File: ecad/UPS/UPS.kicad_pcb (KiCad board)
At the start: 4 copper layers, 177.8 x 139.7 mm, 159 parts, among them J1 Barrel_Jack, J2 Conn_01x02_Socket, J3 USB_C_Receptacle_USB2.0_16P, J4 PROG, Q2 Q_PMOS_DGS, Q3 IRLR7843TRPBF, Q6 Q_NMOS_GDS, Q7 Q_NMOS_GDS, Q8 Q_NMOS_GDS, Q9 Q_NMOS_GDS, SW1 SW_Push, SW2 SW_Push, SW3 SW_DPDT_x2, U1 BQ25730RSNR, U2 MPQ5031GRE-0001-AEC1-P, U3 L78L05_SOT89, U4 STM32L152RCT6, U5 AP2112K-3.3TRG1

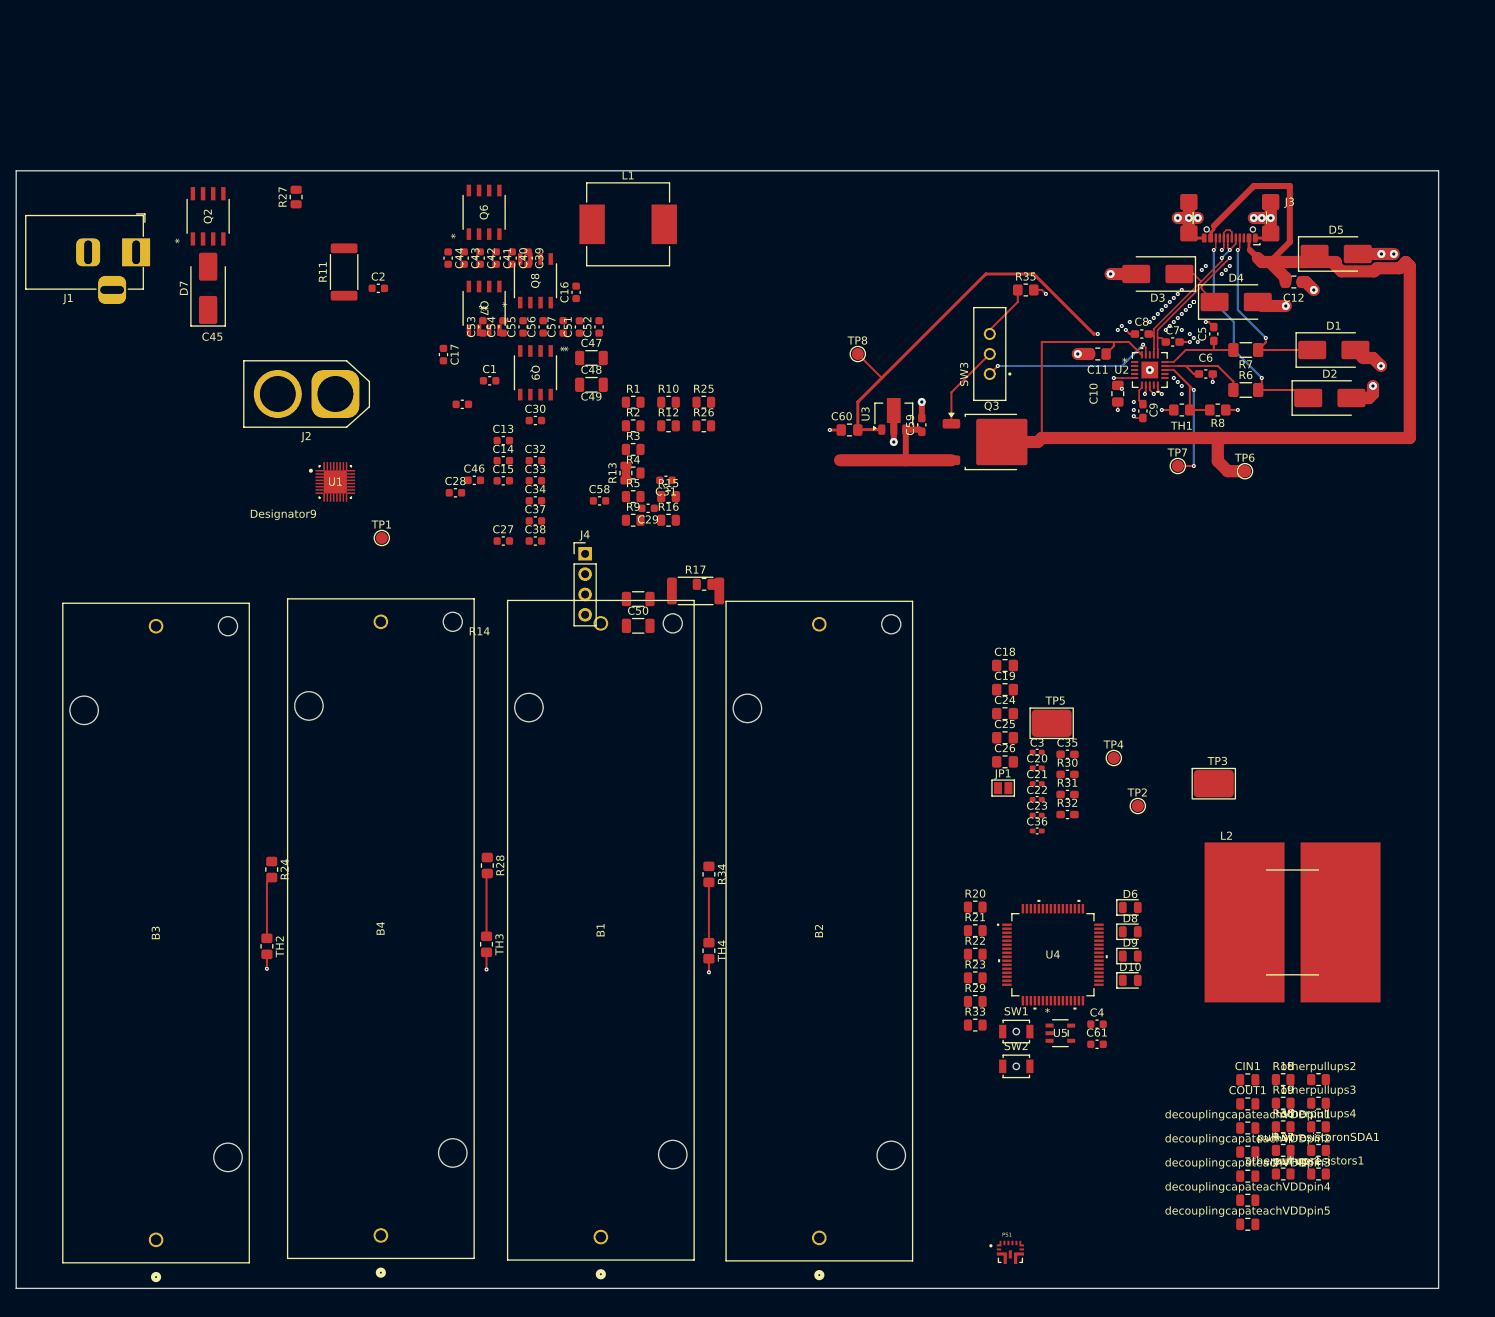
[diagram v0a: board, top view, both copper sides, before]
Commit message: Did some routing, need to figure out how to route to BQ while appeasing DRC
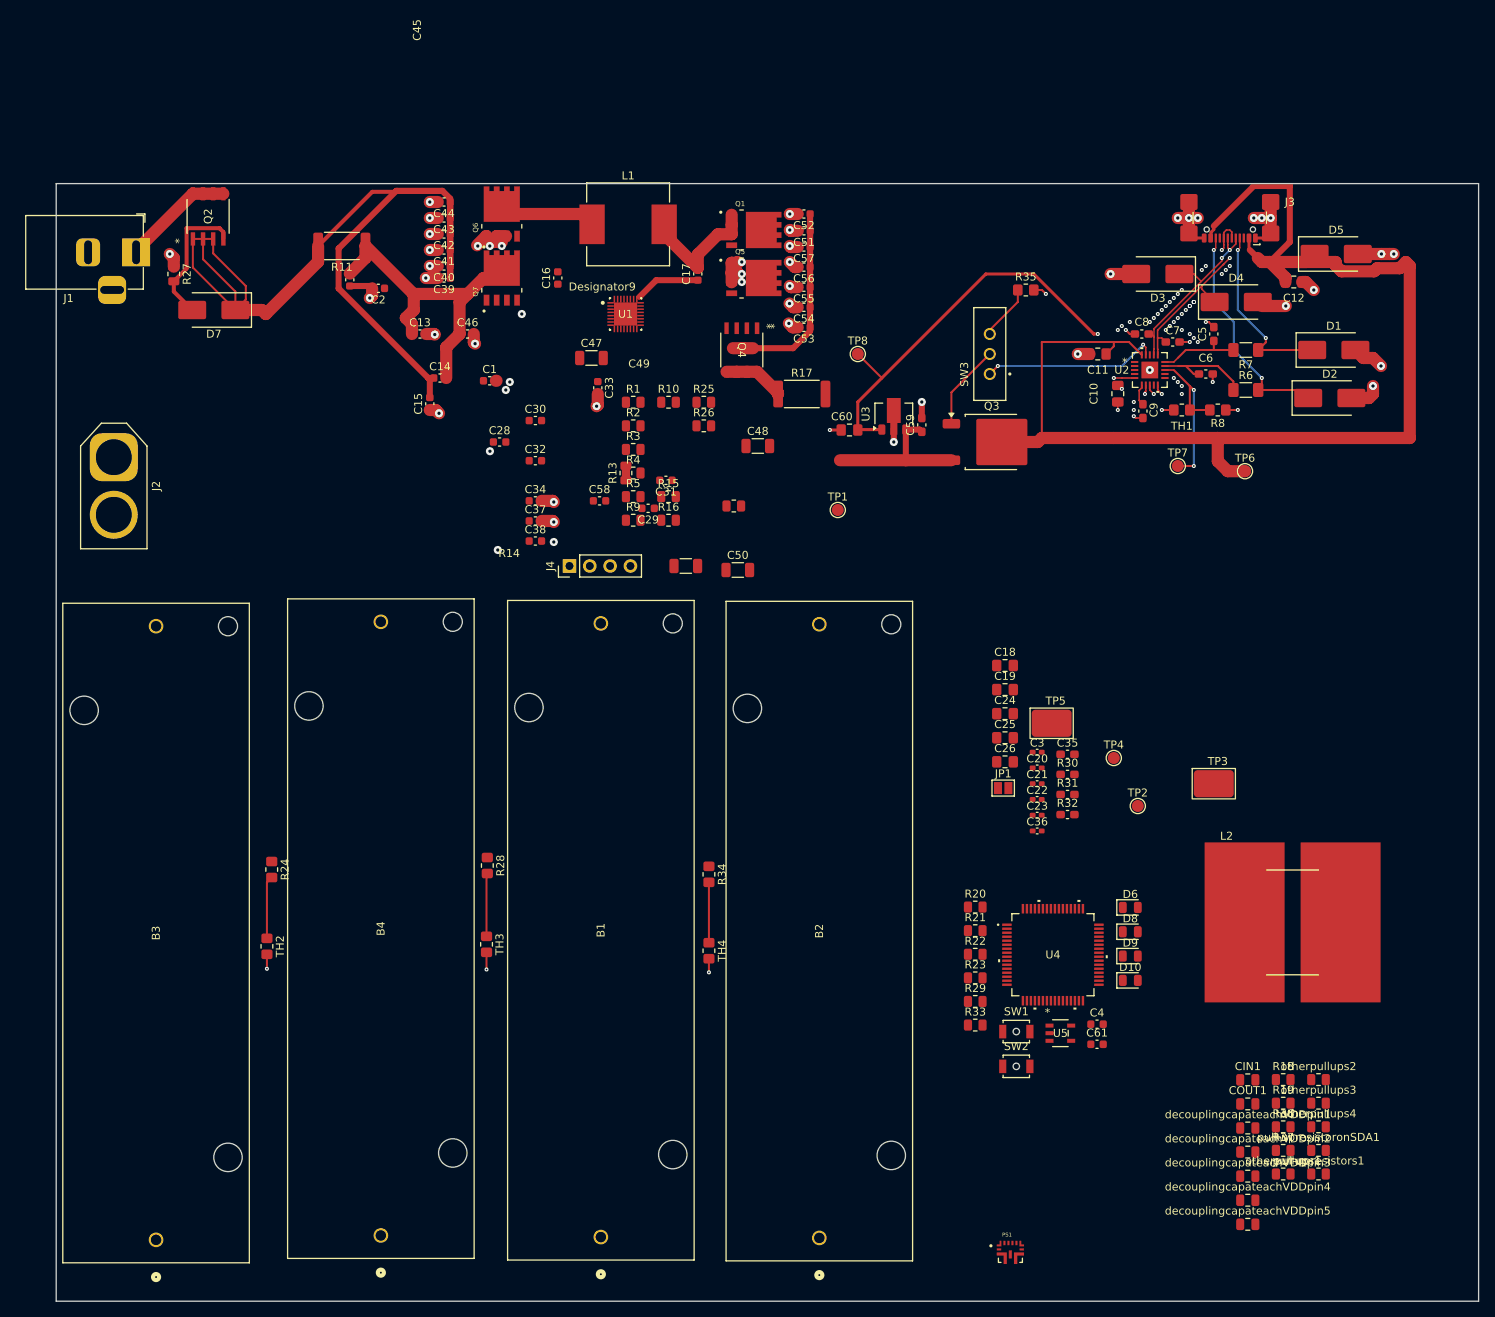
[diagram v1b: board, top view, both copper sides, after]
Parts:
- removed C27: 1uF, Capacitor_SMD:C_0603_1608Metric
- removed Q8, Q9: Q_NMOS_GDS, UPS:Ty's N Channel
- removed R12: 2.2, Resistor_SMD:R_0805_2012Metric
- added Q1: CSD18540Q5B, UPS:TRANS_CSD18540Q5B, F.Cu at (143.0, 45.5)
- added Q4: Q_PMOS_DGS, UPS:FDS6681Z_OSI, F.Cu at (141.5, 60.5)
- added Q5: CSD18540Q5B, UPS:TRANS_CSD18540Q5B, F.Cu at (143.0, 51.5)
- C30: value 680 pF -> 1200 pF
- C31: value 4.7nF -> 3.3nF
- Q6, Q7: value Q_NMOS_GDS -> CSD18540Q5B; footprint UPS:Ty's N Channel -> UPS:TRANS_CSD18540Q5B
- R1: value 191k -> 140k
- R13: value 40.2k -> 16.9k
- R14: value 15k -> 10k
- R2: value 30k -> 10k
- R3: value 380k -> 56k
- R4: value 220k -> 100k
- U1: footprint UPS:RSN0032B-IPC_A -> UPS:RSN0032B-IPC_C
- moved TP1 57.1 mm to (153.5, 80.5)
- moved U1 41.9 mm to (127.0, 56.0)
- moved C53 40.1 mm to (149.3, 57.7), turned to 180 degrees
- moved C54 37.7 mm to (149.3, 55.2), turned to 180 degrees
- moved C55 35.5 mm to (149.3, 52.6), turned to 180 degrees
- moved C56 33.4 mm to (149.3, 50.1), turned to 180 degrees
- moved C17 33.3 mm to (136.0, 51.0), turned to 90 degrees
- moved C57 31.7 mm to (149.3, 47.6), turned to 180 degrees
- moved C51 30.5 mm to (149.3, 45.6), turned to 180 degrees
- moved C52 29.2 mm to (149.3, 43.5), turned to 180 degrees
- moved J2 28.8 mm to (63.0, 73.9), turned to -90 degrees
- moved R17 28.0 mm to (149.0, 66.0)
- moved C48 22.2 mm to (143.5, 72.5)
- moved C45 21.0 mm to (92.5, 51.7), turned to -90 degrees
- moved C46 18.3 mm to (107.2, 58.5)
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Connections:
- C1 pad 2: PGND -> GNDA
- C14 pad 1: Net-(U1-ACP) -> PMOS_IN_GATE
- C15 pad 2: Net-(U1-ACP) -> PMOS_IN_GATE
- C2 pad 2: PGND -> GNDA
- C28 pad 1: PGND -> GNDA
- C29 pad 1: PGND -> GNDA
- C30 pad 1: PGND -> GNDA
- C31 pad 1: PGND -> GNDA
- C32 pad 2: Net-(C32-Pad2) -> Net-(U1-SRP)
- C34 pad 1: Net-(C32-Pad2) -> Net-(U1-SRP)
- C38 pad 2: PGND -> GNDA
- C45 pad 1: Net-(C45-Pad1) -> Net-(U1-ACN)
- C46 pad 1: Net-(C45-Pad1) -> Net-(U1-ACN)
- Q6 pad 2: PMOS_IN_GATE -> PGND
- Q6 pad 3: SW1 -> PGND
- Q6 pad 4: (no net) -> Net-(U1-LODRV1)
- Q7 pad 1: Net-(Q7-G) -> SW1
- Q7 pad 3: PGND -> SW1
- Q7 pad 4: (no net) -> PGND
- R1 pad 2: PGND -> GNDA
- R11 pad 1: Net-(C45-Pad1) -> Net-(U1-ACN)
- R17 pad 1: Net-(C32-Pad2) -> Net-(U1-SRP)
- R2 pad 2: PGND -> GNDA
- R26 pad 2: PGND -> GNDA
- R3 pad 2: PGND -> GNDA
- U1 pad 19: Net-(U1-SRN) -> Net-(J2-Pin_1)
- U1 pad 3: Net-(U1-ACP) -> PMOS_IN_GATE
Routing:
- net PMOS_IN_GATE: track 0.00 -> 131.9 mm
- net Net-(U1-ACN): track 0.00 -> 42.0 mm
- net PGND: track 62.1 -> 101.7 mm, vias 69 -> 99
- net PMOS_OUT_GATE: track 0.00 -> 25.2 mm
- net Net-(D7-A): track 0.00 -> 17.5 mm
- net Net-(U1-SW2): track 0.00 -> 16.6 mm
- net Net-(J1-Pad1): track 0.00 -> 14.1 mm
- net SW1: track 0.00 -> 11.8 mm
- net BTST2: track 0.00 -> 8.16 mm
- net Net-(U1-SRP): track 0.00 -> 7.70 mm
- net (no net): track 0.00 -> 1.00 mm
- net GNDA: track 0.00 -> 0.09 mm, vias 0 -> 3

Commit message: Ty's VBATSENSE Changes
Let me know if I messed this part up, did a small amount
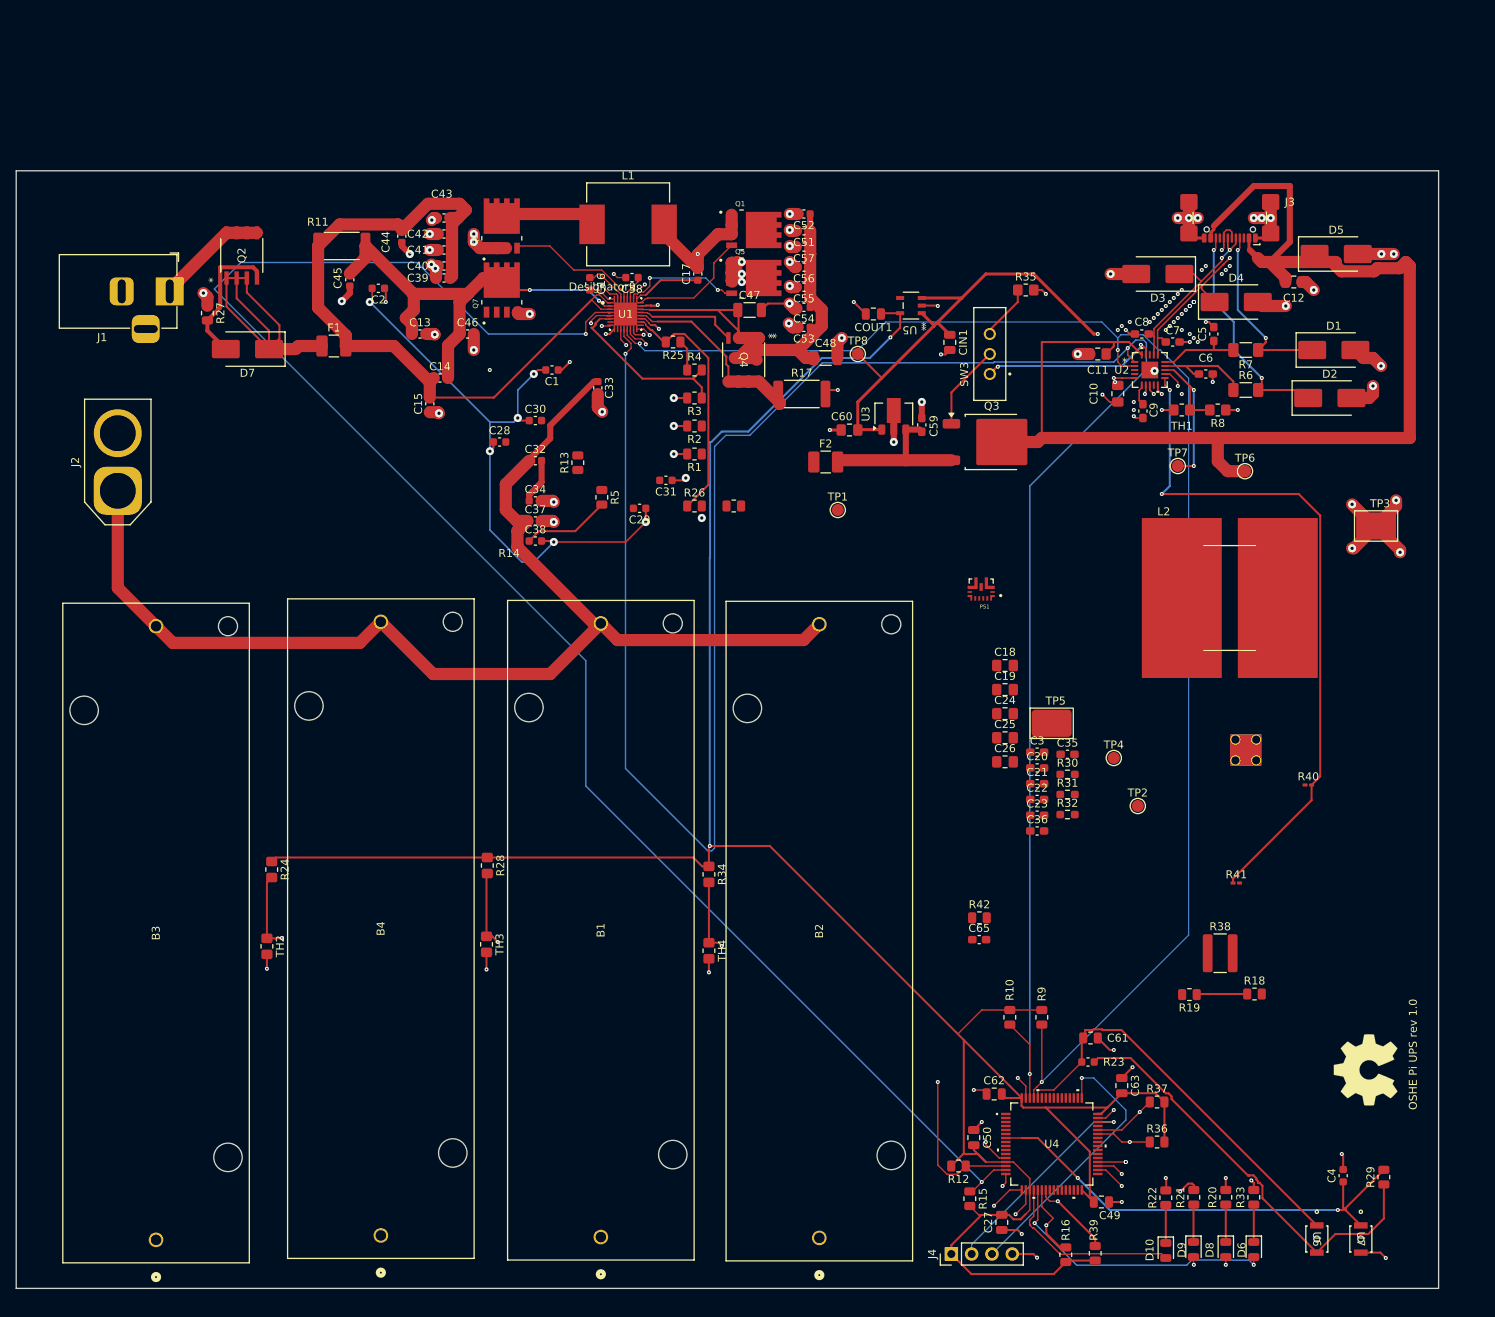
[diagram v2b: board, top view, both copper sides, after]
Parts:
- removed the C49 at (134.5, 87.5)
- removed the C50 at (141.0, 88.0)
- removed JP1: SolderJumper_2_Open, Jumper:SolderJumper-2_P1.3mm_Open_Pad1.0x1.5mm
- removed the R10 at (132.3, 67.0)
- removed the R15 at (132.3, 78.8)
- removed the R16 at (132.3, 81.8)
- removed the R9 at (127.9, 81.8)
- removed SW1, SW2: SW_Push, Button_Switch_SMD:SW_SPST_B3U-1000P-B
- added C65: 1nF, Capacitor_SMD:C_0603_1608Metric_Pad1.08x0.95mm_HandSolder, F.Cu at (171.2, 134.2)
- added F1: PTC 5.5A, Fuse:Fuse_1210_3225Metric_Pad1.42x2.65mm_HandSolder, F.Cu at (90.5, 60.0)
- added F2: PTC 5.5A, Fuse:Fuse_1210_3225Metric_Pad1.42x2.65mm_HandSolder, F.Cu at (152.0, 74.5)
- added NT1: NetTie_3, NetTie:NetTie-4_THT_Pad1.0mm, F.Cu at (203.2, 109.2)
- added R38: 0, Resistor_SMD:R_1218_3246Metric_Pad1.22x4.75mm_HandSolder, F.Cu at (201.3, 135.9)
- added R40: 16.9k, Resistor_SMD:R_0201_0603Metric_Pad0.64x0.40mm_HandSolder, F.Cu at (212.3, 114.9)
- added R41: 10k, Resistor_SMD:R_0201_0603Metric_Pad0.64x0.40mm_HandSolder, F.Cu at (203.3, 127.1)
- added R42: 4.7k, Resistor_SMD:R_0805_2012Metric, F.Cu at (171.2, 131.5)
- added REF**: OSHW-Symbol_8.9x8mm_SilkScreen, Symbol:OSHW-Symbol_8.9x8mm_SilkScreen, F.Cu at (219.5, 150.5)
- added U6: BOOT0, UPS:B3U-1000P-B, F.Cu at (213.4, 171.6)
- added U7: NRST, UPS:B3U-1000P-B, F.Cu at (218.9, 171.6)
- C20, C21, C22, C23, C3, C36: footprint Capacitor_SMD:C_0402_1005Metric_Pad0.74x0.62mm_HandSolder -> Capacitor_SMD:C_0603_1608Metric_Pad1.08x0.95mm_HandSolder
- D7: value D_Zener -> 6V
- R30, R31, R32: footprint Capacitor_SMD:C_0603_1608Metric_Pad1.08x0.95mm_HandSolder -> Resistor_SMD:R_0603_1608Metric_Pad0.98x0.95mm_HandSolder
- moved COUT1 109.3 mm to (157.9, 56.0), turned to 180 degrees
- moved CIN1 99.4 mm to (167.5, 59.5), turned to -90 degrees
- moved J4 98.4 mm to (167.7, 173.5)
- moved U5 92.8 mm to (162.6, 55.0), turned to 180 degrees
- moved PS1 83.0 mm to (171.4, 90.4), turned to 180 degrees
- moved R29 55.6 mm to (221.8, 163.9), turned to 90 degrees
- moved R20 47.9 mm to (202.0, 166.4), turned to 90 degrees
- moved R15 46.1 mm to (170.0, 166.6), turned to -90 degrees
- moved D6 45.5 mm to (205.5, 172.9), turned to -90 degrees
- moved R21 43.1 mm to (198.0, 166.4), turned to 90 degrees
- moved R10 42.0 mm to (175.0, 143.9), turned to -90 degrees
- moved D8 41.5 mm to (202.0, 172.9), turned to -90 degrees
- moved L2 41.3 mm to (202.5, 91.5)
- moved R33 40.9 mm to (205.5, 166.4), turned to 90 degrees
- moved R12 40.6 mm to (168.6, 162.5), turned to 180 degrees
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- renumbered decouplingcapateachVDDpin1 to C27, decouplingcapateachVDDpin2 to C49, decouplingcapateachVDDpin3 to C50, decouplingcapateachVDDpin4 to C62, decouplingcapateachVDDpin5 to C63, pull-upresistoronSDA1 to R10, otherpullups1 to R12, otherpullups2 to R15, otherpullups3 to R16, otherpullups4 to R39, pull-upresistors1 to R9
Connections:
- net Net-(J2-Pin_1) renamed /Charger/VBAT_SENSE
- C14 pad 1: PMOS_IN_GATE -> /Charger/Charger_VBUS_IN
- C15 pad 2: PMOS_IN_GATE -> /Charger/Charger_VBUS_IN
- C24 pad 1: /Output/VBUS_in -> /BoostConvertor/vbus
- C25 pad 1: /Output/VBUS_in -> /BoostConvertor/vbus
- C26 pad 1: /Output/VBUS_in -> /BoostConvertor/vbus
- C27 pad 2: 3.3V -> +3.3V
- C3 pad 1: /Output/VBUS_in -> /BoostConvertor/vbus
- C39 pad 1: PMOS_IN_GATE -> /Charger/Charger_VBUS_IN
- C40 pad 1: PMOS_IN_GATE -> /Charger/Charger_VBUS_IN
- C41 pad 1: PMOS_IN_GATE -> /Charger/Charger_VBUS_IN
- C42 pad 1: PMOS_IN_GATE -> /Charger/Charger_VBUS_IN
- C43 pad 1: PMOS_IN_GATE -> /Charger/Charger_VBUS_IN
- C44 pad 1: PMOS_IN_GATE -> /Charger/Charger_VBUS_IN
- C49 pad 2: 3.3V -> +3.3V
- C50 pad 2: 3.3V -> +3.3V
- C59 pad 1: /Output/VBUS_in -> /Output/VBUS_fused
- C62 pad 2: 3.3V -> +3.3V
- C63 pad 2: 3.3V -> +3.3V
- COUT1 pad 1: 3.3V -> +3.3V
- PS1 pad 5: /Output/VBUS_in -> /BoostConvertor/vbus
- Q3 pad 3: /Output/VBUS_in -> /Output/VBUS_fused
- R10 pad 1: 3.3V -> +3.3V
- R11 pad 2: PMOS_IN_GATE -> /Charger/Charger_VBUS_IN
- R12 pad 2: 3.3V -> +3.3V
- R15 pad 2: 3.3V -> +3.3V
- R16 pad 2: 3.3V -> +3.3V
- R19 pad 2: 3.3V -> +3.3V
- R32 pad 1: /Output/VBUS_in -> /BoostConvertor/vbus
- R36 pad 1: /controller/vsel1 -> /Output/vsel1
- R36 pad 2: 3.3V -> +3.3V
- R37 pad 1: /controller/vsel2 -> /Output/vsel2
- R37 pad 2: 3.3V -> +3.3V
- R39 pad 2: 3.3V -> +3.3V
- R9 pad 1: 3.3V -> +3.3V
- TP1 pad 1: /Output/VBUS_in -> /BoostConvertor/vbus
- U1 pad 1: PMOS_IN_GATE -> /Charger/Charger_VBUS_IN
- U1 pad 3: PMOS_IN_GATE -> /Charger/Charger_VBUS_IN
- U2 pad 11: /Output/vbat_sense -> Net-(U2-GPIO2)
- U3 pad 3: /Output/VBUS_in -> /Output/VBUS_fused
- U4 pad 13: 3.3V -> +3.3V
- U4 pad 19: 3.3V -> +3.3V
- U4 pad 20: Net-(D10-A) -> Net-(U4B-PA4)
- U4 pad 21: Net-(D6-A) -> unconnected-(U4B-PA5-Pad21)
- U4 pad 32: 3.3V -> +3.3V
- U4 pad 41: unconnected-(U4B-PA8-Pad41) -> Net-(D10-A)
- U4 pad 42: unconnected-(U4B-PA9-Pad42) -> Net-(D6-A)
- U4 pad 43: /controller/vsel1 -> /Output/vsel1
- U4 pad 44: /controller/vsel2 -> /Output/vsel2
- U4 pad 48: 3.3V -> +3.3V
- U4 pad 64: 3.3V -> +3.3V
- U5 pad 5: 3.3V -> +3.3V
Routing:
- net +3.3V: track 0.00 -> 319.0 mm, vias 0 -> 2
- net /Output/SDA: track 0.00 -> 290.7 mm, vias 0 -> 3
- net /Charger/chrg_ok: track 0.00 -> 213.6 mm, vias 0 -> 2
- net /Output/SCL: track 0.00 -> 187.1 mm, vias 0 -> 3
- net /Charger/VBAT_SENSE: track 0.00 -> 183.4 mm, vias 0 -> 2
- net /Charger/bat_th1: track 7.85 -> 188.6 mm, vias 0 -> 2
- net /Charger/OTG/VAP: track 0.00 -> 153.5 mm, vias 0 -> 2
- net /Charger/bat_th2: track 7.89 -> 155.2 mm, vias 0 -> 2
- net /Charger/cmp_out: track 0.00 -> 142.0 mm, vias 0 -> 2
- net /Charger/PROCHOT_N: track 0.00 -> 130.5 mm, vias 0 -> 2
- net /Output/vsel2: track 0.00 -> 114.8 mm, vias 0 -> 2
- net /Charger/bat_th3: track 7.55 -> 120.9 mm, vias 0 -> 3
- net /Charger/Charger_VBUS_IN: track 0.00 -> 91.8 mm
- net PMOS_IN_GATE: track 131.9 -> 42.1 mm
- net Net-(U2-GPIO2): track 0.00 -> 86.5 mm, vias 0 -> 2
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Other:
- board text added: "OSHE Pi UPS rev 1.0"

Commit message: More routing, almost done but Ty works til 5
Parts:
- moved R38 55.5 mm to (156.3, 103.4), turned to 180 degrees
- moved C24 31.8 mm to (201.7, 89.5)
- moved C25 31.8 mm to (201.7, 92.5)
- moved C26 31.8 mm to (201.7, 95.5)
- moved L2 28.0 mm to (174.5, 90.0)
- moved C3 25.7 mm to (201.7, 99.8)
- moved TP5 23.1 mm to (186.4, 82.5), turned to 90 degrees
- moved C36 21.8 mm to (193.4, 104.8), turned to -90 degrees
- moved R32 19.8 mm to (191.3, 101.0), turned to 90 degrees
- moved C23 19.0 mm to (191.4, 104.8), turned to -90 degrees
- moved PS1 17.8 mm to (189.1, 92.4), turned to 90 degrees
- moved R31 16.5 mm to (188.8, 101.0), turned to -90 degrees
- moved C22 16.2 mm to (189.4, 104.8), turned to 90 degrees
- moved C19 6.96 mm to (168.0, 105.7), turned to -90 degrees
- moved C18 6.66 mm to (171.0, 105.7), turned to -90 degrees
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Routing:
- net PMOS_OUT_GATE: track 62.7 -> 107.7 mm
- net Net-(C30-Pad2): track 0.00 -> 41.7 mm
- net Net-(PS1-VIN): track 0.00 -> 37.0 mm
- net /BoostConvertor/vbus: track 0.00 -> 28.0 mm
- net GNDA: track 84.5 -> 110.1 mm
- net PGND: track 180.0 -> 201.7 mm, vias 121 -> 130
- net VDDA: track 14.8 -> 33.9 mm, vias 0 -> 3
- net +3.3V: track 319.0 -> 334.6 mm, vias 2 -> 4
